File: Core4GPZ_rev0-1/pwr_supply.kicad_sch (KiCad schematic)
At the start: 3 parts

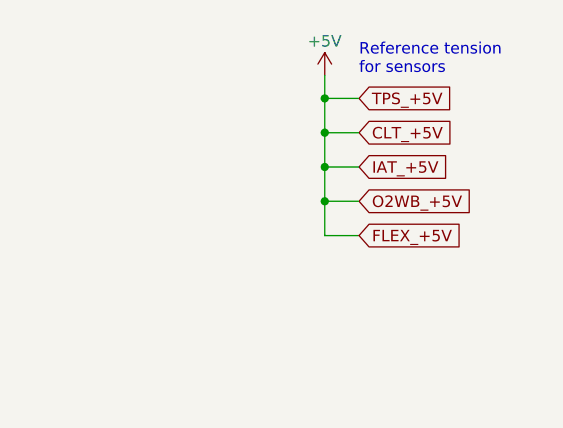
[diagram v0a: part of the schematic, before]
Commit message: Rewied ground plane, set all SNSR+5V ref to one pin
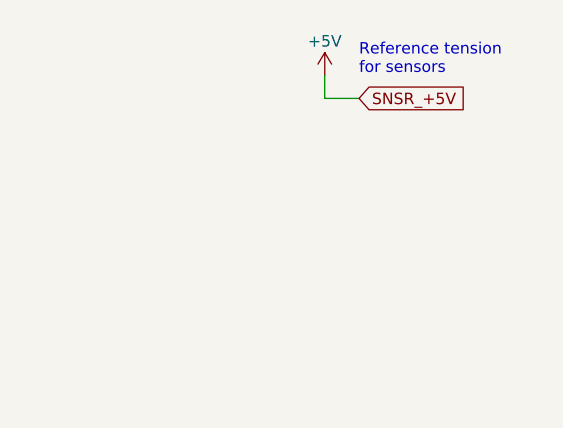
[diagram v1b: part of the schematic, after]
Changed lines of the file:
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@@
-	)
-	(junction
-		(at 130.81 52.07)
-		(diameter 0)
-		(color 0 0 0 0)
-	)
-	(junction
-		(at 130.81 44.45)
-		(diameter 0)
-		(color 0 0 0 0)
 	)
 	(junction
@@
 		(color 0 0 0 0)
 	)
-	(junction
-		(at 130.81 55.88)
-		(diameter 0)
-		(color 0 0 0 0)
-	)
-	(junction
-		(at 130.81 48.26)
-		(diameter 0)
-		(color 0 0 0 0)
-	)
 	(wire
 		(pts
@@
 	(wire
 		(pts
-			(xy 130.81 52.07) (xy 134.62 52.07)
-		)
-		(stroke
-			(width 0)
-			(type default)
-		)
-	)
-	(wire
-		(pts
 			(xy 64.77 54.61) (xy 64.77 59.69)
 		)
@@
 	(wire
 		(pts
-			(xy 130.81 52.07) (xy 130.81 55.88)
-		)
-		(stroke
-			(width 0)
-			(type default)
-		)
-	)
-	(wire
-		(pts
 			(xy 55.88 54.61) (xy 55.88 59.69)
 		)
@@
 	(wire
 		(pts
-			(xy 130.81 55.88) (xy 130.81 59.69)
-		)
-		(stroke
-			(width 0)
-			(type default)
-		)
-	)
-	(wire
-		(pts
-			(xy 130.81 44.45) (xy 130.81 48.26)
-		)
-		(stroke
-			(width 0)
-			(type default)
-		)
-	)
-	(wire
-		(pts
 			(xy 64.77 44.45) (xy 72.39 44.45)
 		)
@@
 		(pts
 			(xy 72.39 41.91) (xy 72.39 44.45)
-		)
-		(stroke
-			(width 0)
-			(type default)
-		)
-	)
-	(wire
-		(pts
-			(xy 130.81 55.88) (xy 134.62 55.88)
-		)
-		(stroke
-			(width 0)
-			(type default)
-		)
-	)
-	(wire
-		(pts
-			(xy 130.81 59.69) (xy 134.62 59.69)
-		)
-		(stroke
-			(width 0)
-			(type default)
-		)
-	)
-	(wire
-		(pts
-			(xy 130.81 48.26) (xy 134.62 48.26)
-		)
-		(stroke
-			(width 0)
-			(type default)
-		)
-	)
-	(wire
-		(pts
-			(xy 130.81 48.26) (xy 130.81 52.07)
 		)
 		(stroke
@@
 		)
 	)
-	(global_label "FLEX_+5V"
-		(shape input)
-		(at 134.62 59.69 0)
+	(global_label "INJ_+12V"
+		(shape input)
+		(at 77.47 44.45 0)
 		(fields_autoplaced yes)
 		(effects
@@
 		)
 		(property "Intersheetrefs" "${INTERSHEET_REFS}"
-			(at 146.9185 59.69 0)
+			(at 89.4057 44.45 0)
 			(effects
 				(font
@@
 		)
 	)
-	(global_label "INJ_+12V"
-		(shape input)
-		(at 77.47 44.45 0)
-		(fields_autoplaced yes)
-		(effects
-			(font
-				(size 1.27 1.27)
-			)
-			(justify left)
-		)
-		(property "Intersheetrefs" "${INTERSHEET_REFS}"
-			(at 89.4057 44.45 0)
-			(effects
-				(font
-					(size 1.27 1.27)
-				)
-				(justify left)
-				(hide yes)
-			)
-		)
-	)
-	(global_label "CLT_+5V"
-		(shape input)
-		(at 134.62 48.26 0)
-		(fields_autoplaced yes)
-		(effects
-			(font
-				(size 1.27 1.27)
-			)
-			(justify left)
-		)
-		(property "Intersheetrefs" "${INTERSHEET_REFS}"
-			(at 145.709 48.26 0)
-			(effects
-				(font
-					(size 1.27 1.27)
-				)
-				(justify left)
-				(hide yes)
-			)
-		)
-	)
-	(global_label "IAT_+5V"
-		(shape input)
-		(at 134.62 52.07 0)
-		(fields_autoplaced yes)
-		(effects
-			(font
-				(size 1.27 1.27)
-			)
-			(justify left)
-		)
-		(property "Intersheetrefs" "${INTERSHEET_REFS}"
-			(at 145.1043 52.07 0)
-			(effects
-				(font
-					(size 1.27 1.27)
-				)
-				(justify left)
-				(hide yes)
-			)
-		)
-	)
 	(global_label "BIKE_GROUND"
 		(shape input)
@@
 		)
 	)
-	(global_label "O2WB_+5V"
-		(shape input)
-		(at 134.62 55.88 0)
-		(fields_autoplaced yes)
-		(effects
-			(font
-				(size 1.27 1.27)
-			)
-			(justify left)
-		)
-		(property "Intersheetrefs" "${INTERSHEET_REFS}"
-			(at 147.7047 55.88 0)
-			(effects
-				(font
-					(size 1.27 1.27)
-				)
-				(justify left)
-				(hide yes)
-			)
-		)
-	)
 	(global_label "BIKE_+12V_SWITCHED_IN"
 		(shape input)
@@
 		)
 	)
-	(global_label "TPS_+5V"
+	(global_label "SNSR_+5V"
 		(shape input)
 		(at 134.62 44.45 0)
@@
 		)
 		(property "Intersheetrefs" "${INTERSHEET_REFS}"
-			(at 145.8904 44.45 0)
-			(effects
-				(font
+			(at 147.4628 44.45 0)
+			(effects
+				(font

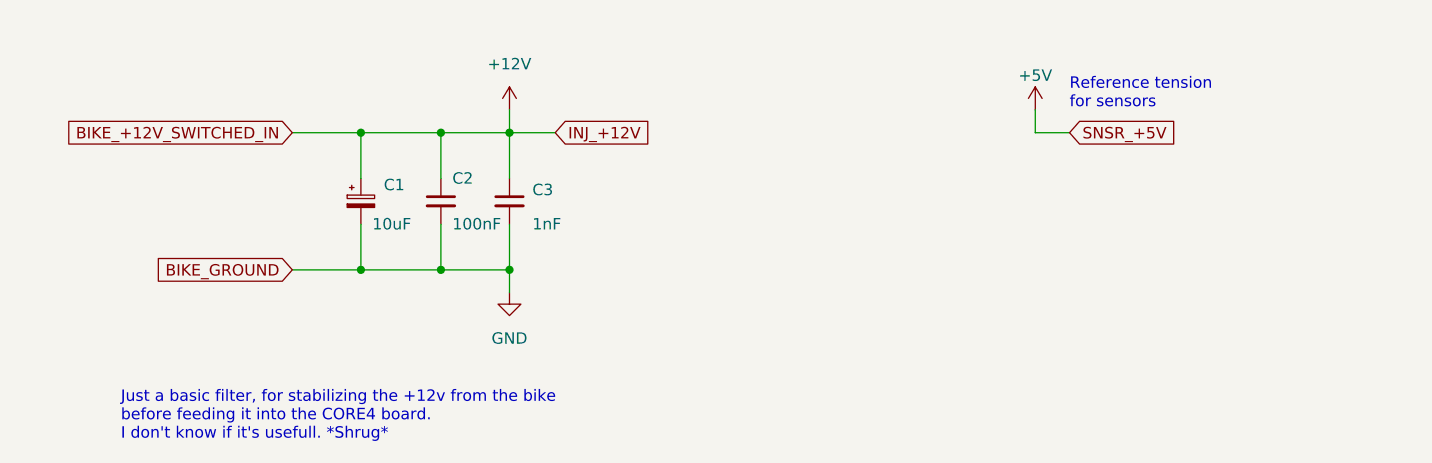
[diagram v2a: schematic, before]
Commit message: Moved +12V decoupling capacitors
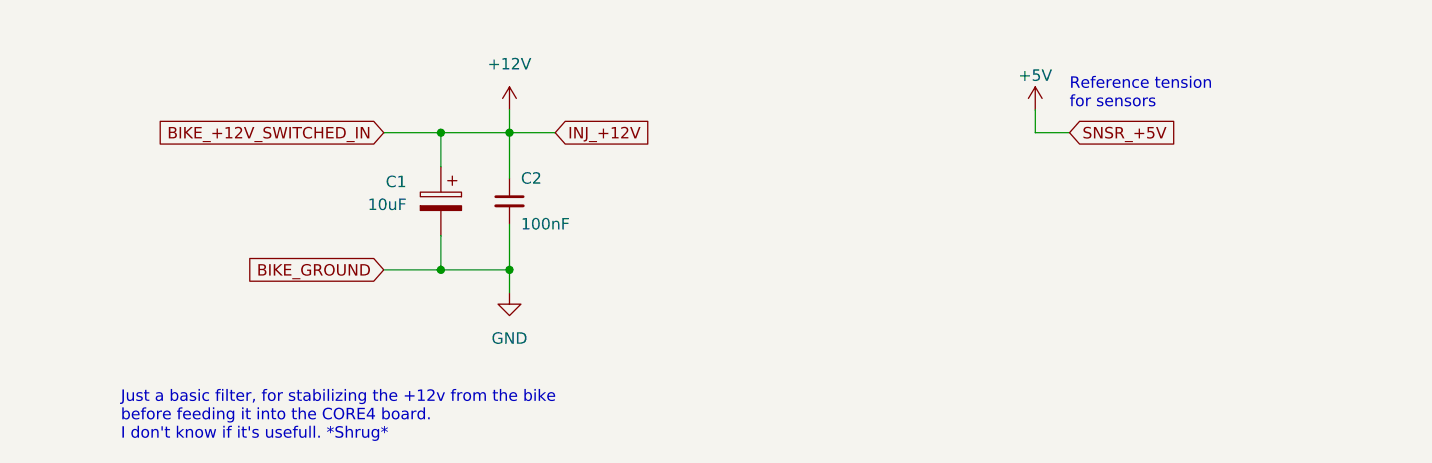
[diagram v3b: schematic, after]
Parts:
- removed C1: 10uF, Capacitor_THT:CP_Radial_D5.0mm_P2.00mm, symbol Device:C_Polarized_Small
- removed C3: 1nF, Capacitor_SMD:C_1206_3216Metric_Pad1.33x1.80mm_HandSolder, symbol Device:C_Small
- added C1: 10uF, Capacitor_THT:CP_Radial_D5.0mm_P2.50mm, symbol Device:C_Polarized
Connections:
- net +12V: now also C1.1
- net GND: now also C1.2
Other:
- moved on the sheet: C2
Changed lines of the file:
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@@
 	(paper "A4")
-	(junction
-		(at 55.88 44.45)
-		(diameter 0)
-		(color 0 0 0 0)
-	)
 	(junction
 		(at 72.39 44.45)
@@
 	)
 	(junction
+		(at 72.39 59.69)
+		(diameter 0)
+		(color 0 0 0 0)
+	)
+	(junction
 		(at 64.77 59.69)
 		(diameter 0)
 		(color 0 0 0 0)
 	)
-	(junction
-		(at 55.88 59.69)
-		(diameter 0)
-		(color 0 0 0 0)
-	)
-	(junction
-		(at 72.39 59.69)
-		(diameter 0)
-		(color 0 0 0 0)
-	)
-	(wire
-		(pts
-			(xy 48.26 59.69) (xy 55.88 59.69)
-		)
-		(stroke
-			(width 0)
-			(type default)
-		)
-	)
-	(wire
-		(pts
-			(xy 64.77 54.61) (xy 64.77 59.69)
-		)
-		(stroke
-			(width 0)
-			(type default)
-		)
-	)
 	(wire
 		(pts
@@
 	(wire
 		(pts
-			(xy 55.88 54.61) (xy 55.88 59.69)
+			(xy 64.77 59.69) (xy 72.39 59.69)
 		)
 		(stroke
@@
 	(wire
 		(pts
-			(xy 48.26 44.45) (xy 55.88 44.45)
-		)
-		(stroke
-			(width 0)
-			(type default)
-		)
-	)
-	(wire
-		(pts
-			(xy 55.88 44.45) (xy 55.88 49.53)
-		)
-		(stroke
-			(width 0)
-			(type default)
-		)
-	)
-	(wire
-		(pts
-			(xy 55.88 44.45) (xy 64.77 44.45)
+			(xy 64.77 55.88) (xy 64.77 59.69)
+		)
+		(stroke
+			(width 0)
+			(type default)
+		)
+	)
+	(wire
+		(pts
+			(xy 58.42 44.45) (xy 64.77 44.45)
 		)
 		(stroke
@@
 	(wire
 		(pts
-			(xy 64.77 59.69) (xy 72.39 59.69)
-		)
-		(stroke
-			(width 0)
-			(type default)
-		)
-	)
-	(wire
-		(pts
-			(xy 64.77 44.45) (xy 64.77 49.53)
-		)
-		(stroke
-			(width 0)
-			(type default)
-		)
-	)
-	(wire
-		(pts
-			(xy 55.88 59.69) (xy 64.77 59.69)
+			(xy 58.42 59.69) (xy 64.77 59.69)
+		)
+		(stroke
+			(width 0)
+			(type default)
+		)
+	)
+	(wire
+		(pts
+			(xy 64.77 44.45) (xy 64.77 48.26)
 		)
 		(stroke
@@
 	(global_label "BIKE_GROUND"
 		(shape input)
-		(at 48.26 59.69 180)
+		(at 58.42 59.69 180)
 		(fields_autoplaced yes)
 		(effects
@@
 		)
 		(property "Intersheetrefs" "${INTERSHEET_REFS}"
-			(at 32.2119 59.69 0)
+			(at 42.3719 59.69 0)
 			(effects
 				(font
@@
 	(global_label "BIKE_+12V_SWITCHED_IN"
 		(shape input)
-		(at 48.26 44.45 180)
+		(at 58.42 44.45 180)
 		(fields_autoplaced yes)
 		(effects
@@
 		)
 		(property "Intersheetrefs" "${INTERSHEET_REFS}"
-			(at 21.8101 44.45 0)
+			(at 31.9701 44.45 0)
 			(effects
 				(font
@@
 	(symbol
 		(lib_id "Device:C_Small")
-		(at 64.77 52.07 0)
+		(at 72.39 52.07 0)
 		(unit 1)
 		(exclude_from_sim no)
@@
 		(dnp no)
 		(property "Reference" "C2"
-			(at 66.04 49.53 0)
+			(at 73.66 49.53 0)
 			(effects
 				(font
@@
 		)
 		(property "Value" "100nF"
-			(at 66.04 54.61 0)
+			(at 73.66 54.61 0)
 			(effects
 				(font
@@
 		)
 		(property "Footprint" "Capacitor_SMD:C_1206_3216Metric_Pad1.33x1.80mm_HandSolder"
-			(at 64.77 52.07 0)
+			(at 72.39 52.07 0)
 			(effects
 				(font
@@
 		)
 		(property "Datasheet" "~"
-			(at 64.77 52.07 0)
+			(at 72.39 52.07 0)
 			(effects
 				(font
@@
 		)
 		(property "Description" ""
-			(at 64.77 52.07 0)
+			(at 72.39 52.07 0)
 			(effects
 				(font
@@
 				(path "/ac28f42d-34b3-4fcc-84dd-ab6106f99610/daf77dd8-6c93-40bb-b740-2abe26fd61d2"
 					(reference "C2")
-					(unit 1)
-				)
-			)
-		)
-	)
-	(symbol
-		(lib_id "Device:C_Small")
-		(at 72.39 52.07 0)
-		(unit 1)
-		(exclude_from_sim no)
-		(in_bom yes)
-		(on_board yes)
-		(dnp no)
-		(property "Reference" "C3"
-			(at 74.93 50.8063 0)
-			(effects
-				(font
-					(size 1.27 1.27)
-				)
-				(justify left)
-			)
-		)
-		(property "Value" "1nF"
-			(at 74.93 54.61 0)
-			(effects
-				(font
-					(size 1.27 1.27)
-				)
-				(justify left)
-			)
-		)
-		(property "Footprint" "Capacitor_SMD:C_1206_3216Metric_Pad1.33x1.80mm_HandSolder"
-			(at 72.39 52.07 0)
-			(effects
-				(font
-					(size 1.27 1.27)
-				)
-				(hide yes)
-			)
-		)
-		(property "Datasheet" "~"
-			(at 72.39 52.07 0)
-			(effects
-				(font
-					(size 1.27 1.27)
-				)
-				(hide yes)
-			)
-		)
-		(property "Description" ""
-			(at 72.39 52.07 0)
-			(effects
-				(font
-					(size 1.27 1.27)
-				)
-				(hide yes)
-			)
-		)
-		(pin "1"
-		)
-		(pin "2"
-		)
-		(instances
-			(project "Core4GPZ_rev0-1"
-				(path "/ac28f42d-34b3-4fcc-84dd-ab6106f99610/daf77dd8-6c93-40bb-b740-2abe26fd61d2"
-					(reference "C3")
 					(unit 1)
 				)
@@
 	)
 	(symbol
-		(lib_id "Device:C_Polarized_Small")
-		(at 55.88 52.07 0)
+		(lib_id "Device:C_Polarized")
+		(at 64.77 52.07 0)
+		(mirror y)
 		(unit 1)
 		(exclude_from_sim no)
@@
 		(dnp no)
 		(property "Reference" "C1"
-			(at 58.42 50.2539 0)
+			(at 60.96 49.9109 0)
 			(effects
 				(font
@@
 		)
 		(property "Value" "10uF"
-			(at 57.15 54.61 0)
+			(at 60.96 52.4509 0)
 			(effects
 				(font
@@
 			)
 		)
-		(property "Footprint" "Capacitor_THT:CP_Radial_D5.0mm_P2.00mm"
-			(at 55.88 52.07 0)
+		(property "Footprint" "Capacitor_THT:CP_Radial_D5.0mm_P2.50mm"
+			(at 63.8048 55.88 0)
 			(effects
 				(font
@@
 		)
 		(property "Datasheet" "~"
-			(at 55.88 52.07 0)
-			(effects
-				(font
-					(size 1.27 1.27)
-				)
-				(hide yes)
-			)
-		)
-		(property "Description" ""
-			(at 55.88 52.07 0)
-			(effects
-				(font
-					(size 1.27 1.27)
-				)
-				(hide yes)
-			)
+			(at 64.77 52.07 0)
+			(effects
+				(font
+					(size 1.27 1.27)
+				)
+				(hide yes)
+			)
+		)
+		(property "Description" "Polarized capacitor"
+			(at 64.77 52.07 0)
+			(effects
+				(font
+					(size 1.27 1.27)
+				)
+				(hide yes)
+			)
+		)
+		(pin "1"
 		)
 		(pin "2"
 		)
-		(pin "1"
-		)
 		(instances
-			(project "Core4GPZ_rev0-1"
+			(project ""
 				(path "/ac28f42d-34b3-4fcc-84dd-ab6106f99610/daf77dd8-6c93-40bb-b740-2abe26fd61d2"
 					(reference "C1")

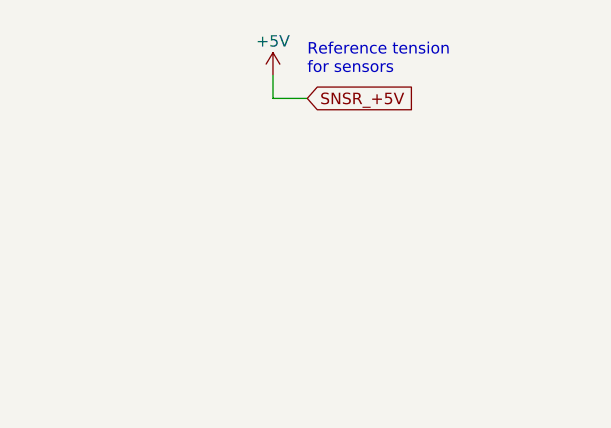
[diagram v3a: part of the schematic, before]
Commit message: Changed MAP sensors for MPXHZ6250AC6T1
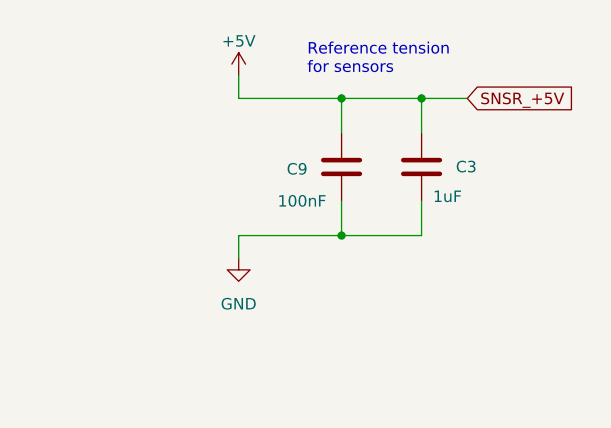
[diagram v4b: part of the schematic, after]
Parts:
- added C3: 1uF, Capacitor_SMD:C_0805_2012Metric_Pad1.18x1.45mm_HandSolder, symbol Device:C
- added C9: 100nF, Capacitor_SMD:C_0805_2012Metric_Pad1.18x1.45mm_HandSolder, symbol Device:C
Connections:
- net +5V: now also C3.1, C9.1
- net GND: now also C3.2, C9.2

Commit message: Modified GND Plane. Reworked routing
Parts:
- renumbered C9 to C3, C3 to C4
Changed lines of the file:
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@@
 		(dnp no)
 		(fields_autoplaced yes)
-		(property "Reference" "#PWR017"
+		(property "Reference" "#PWR013"
 			(at 127 68.58 0)
 			(effects
@@
 			(project "Core4GPZ_rev0-1"
 				(path "/ac28f42d-34b3-4fcc-84dd-ab6106f99610/daf77dd8-6c93-40bb-b740-2abe26fd61d2"
-					(reference "#PWR017")
+					(reference "#PWR013")
 					(unit 1)
 				)
@@
 		(on_board yes)
 		(dnp no)
-		(property "Reference" "C9"
+		(property "Reference" "C3"
 			(at 132.334 52.324 0)
 			(effects
@@
 			(project "Core4GPZ_rev0-1"
 				(path "/ac28f42d-34b3-4fcc-84dd-ab6106f99610/daf77dd8-6c93-40bb-b740-2abe26fd61d2"
-					(reference "C9")
+					(reference "C3")
 					(unit 1)
 				)
@@
 		(on_board yes)
 		(dnp no)
-		(property "Reference" "C3"
+		(property "Reference" "C4"
 			(at 151.13 52.07 0)
 			(effects
@@
 			(project ""
 				(path "/ac28f42d-34b3-4fcc-84dd-ab6106f99610/daf77dd8-6c93-40bb-b740-2abe26fd61d2"
-					(reference "C3")
+					(reference "C4")
 					(unit 1)
 				)

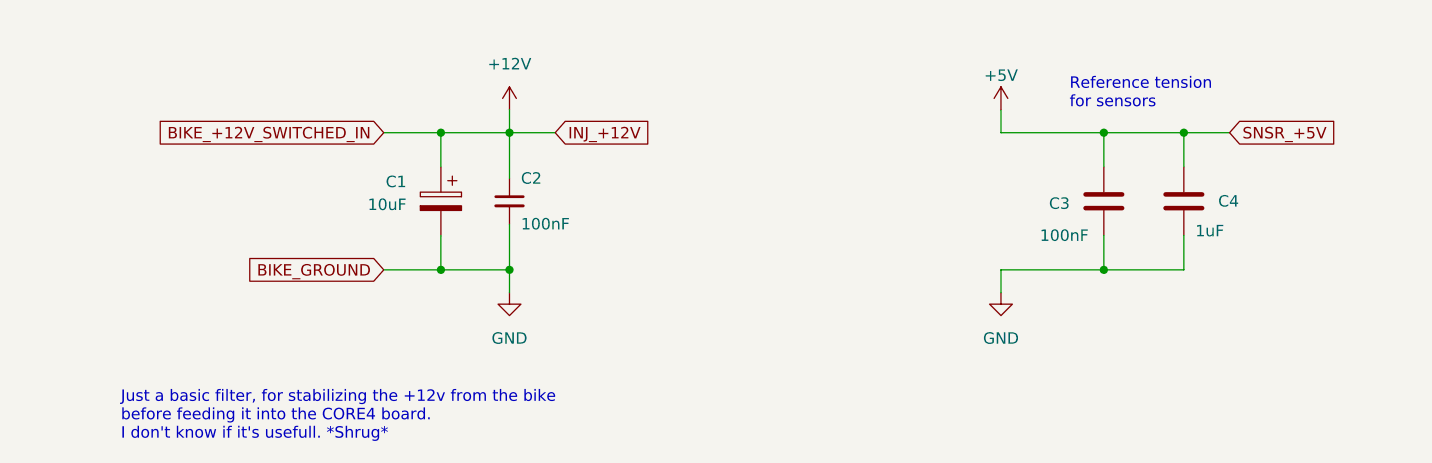
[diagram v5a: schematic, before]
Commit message: Implemented DRV8825 and upgrade IGN Driver
Ignition drivers upgraded with SMD IGBT FGD3440
Added Stepper Driver DRV8825
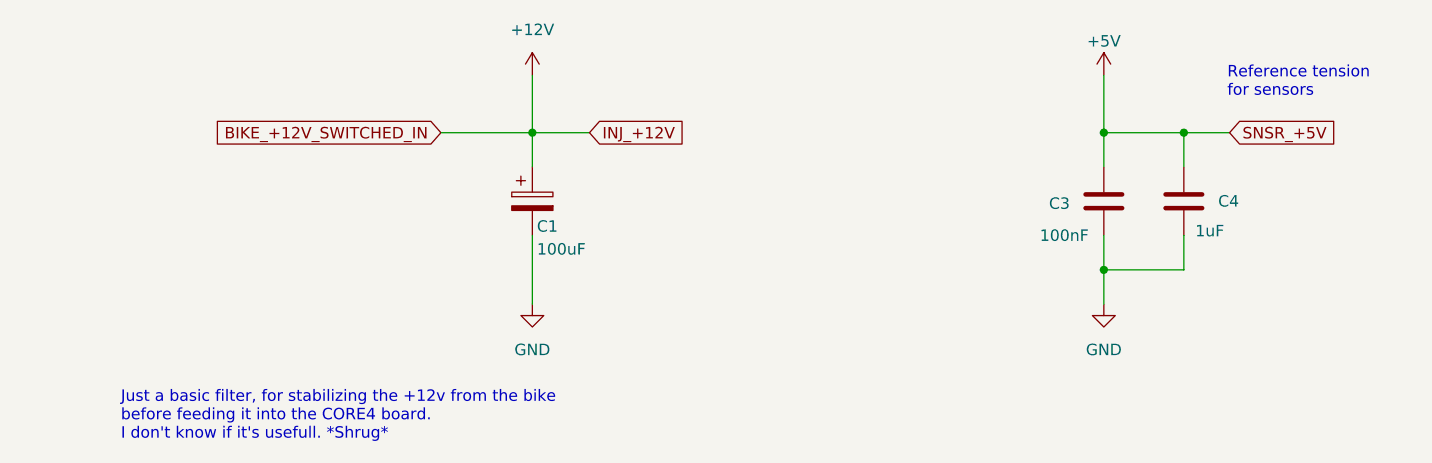
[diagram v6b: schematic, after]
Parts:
- removed C2: 100nF, Capacitor_SMD:C_1206_3216Metric_Pad1.33x1.80mm_HandSolder, symbol Device:C_Small
- C1: value 10uF -> 100uF; footprint Capacitor_THT:CP_Radial_D5.0mm_P2.50mm -> Capacitor_SMD:CP_Elec_6.3x7.7; Voltage (none) -> 24v

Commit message: Removed NeutralSwitch. Added Up-Shifter support
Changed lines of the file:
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@@
 		)
 		(property "Voltage" "24v"
-			(at 74.93 52.07 0)
+			(at 77.216 49.784 0)
 			(effects
 				(font
 					(size 1.27 1.27)
 				)
-				(hide yes)
 			)
 		)
